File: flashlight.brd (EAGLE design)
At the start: 33 x 33 mm, 2 parts

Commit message: version 2 of the top board
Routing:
- net N$5: track 0.00 -> 106.7 mm, vias 1 -> 0
- net N$14: track 0.00 -> 13.2 mm, vias 1 -> 2
- net N$2: track 8.13 -> 0.00 mm
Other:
- board size 33 x 33 mm -> 33.2 x 17.8 mm
- board text added: "Top Board Rev. 2.0"
- board text removed: "Rev. 1.1"
- board text removed: "Top Board Rev. 1.1"
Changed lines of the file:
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@@
 <board>
 <plain>
-<circle x="16.51" y="16.51" radius="16.51" width="0.040640625" layer="20"/>
-<circle x="16.51" y="16.51" radius="14.5542" width="3.937" layer="16"/>
-<circle x="16.51" y="16.51" radius="5.08" width="11.43" layer="30"/>
+<circle x="16.51" y="16.51" radius="1.27" width="11.43" layer="30"/>
 <text x="16.51" y="20.32" size="1.778" layer="25" align="bottom-center">Stockton
 Flashlight</text>
-<circle x="16.51" y="16.51" radius="14.7574" width="3.556" layer="30"/>
-<circle x="16.51" y="16.51" radius="5.08" width="12.7" layer="16"/>
-<rectangle x1="6.35" y1="19.685" x2="26.67" y2="25.4" layer="1"/>
-<rectangle x1="6.35" y1="7.62" x2="26.67" y2="13.335" layer="1"/>
-<text x="16.51" y="3.81" size="1.778" layer="1" align="bottom-center">Rev. 1.1</text>
-<text x="16.51" y="3.81" size="1.778" layer="25" align="bottom-center">Top Board
-Rev. 1.1</text>
+<circle x="16.51" y="16.51" radius="0.762" width="12.7" layer="16"/>
+<rectangle x1="6.35" y1="19.685" x2="26.67" y2="22.86" layer="1"/>
+<rectangle x1="6.35" y1="10.16" x2="26.67" y2="13.335" layer="1"/>
+<text x="16.51" y="9.398" size="1.778" layer="25" align="bottom-center">Top Board
+Rev. 2.0</text>
 <rectangle x1="16" y1="13.2" x2="17" y2="19.7" layer="1"/>
 <text x="19.2" y="14.6" size="1.778" layer="25">+</text>
@@
 <rectangle x1="31.242" y1="15.24" x2="33.02" y2="17.78" layer="1"/>
 <rectangle x1="31.75" y1="15.24" x2="33.02" y2="17.78" layer="29"/>
-<circle x="16.51" y="16.51" radius="14.810615625" width="1.6256" layer="1"/>
+<wire x1="2.54" y1="25.4" x2="2.54" y2="7.62" width="0.0508" layer="20" curve="64.94"/>
+<wire x1="30.48" y1="25.4" x2="30.48" y2="7.62" width="0.0508" layer="20" curve="-65.94"/>
+<wire x1="2.54" y1="25.4" x2="30.48" y2="25.4" width="0.0508" layer="20"/>
+<wire x1="2.54" y1="7.62" x2="30.48" y2="7.62" width="0.0508" layer="20"/>
+<rectangle x1="4.064" y1="7.62" x2="29.21" y2="8.89" layer="1"/>
+<rectangle x1="4.318" y1="24.13" x2="28.702" y2="25.4" layer="1"/>
+<rectangle x1="4.318" y1="24.13" x2="28.702" y2="25.654" layer="16"/>
+<rectangle x1="4.318" y1="7.366" x2="28.702" y2="8.89" layer="16"/>
+<wire x1="4.572" y1="25.4" x2="4.572" y2="7.62" width="3.556" layer="30" curve="73.34"/>
+<wire x1="28.448" y1="25.4" x2="28.448" y2="7.62" width="3.556" layer="30" curve="-73.34"/>
+<rectangle x1="4.318" y1="7.366" x2="28.956" y2="8.89" layer="30"/>
+<rectangle x1="4.318" y1="24.13" x2="28.448" y2="25.654" layer="30"/>
 </plain>
 <attributes>
@@
 </autorouter>
 <elements>
-<element name="R1" library="resistor" package="R2010" value="" x="8.89" y="16.51" rot="R180"/>
+<element name="R1" library="resistor" package="R2010" value="" x="8.89" y="16.51" smashed="yes" rot="R180">
+<attribute name="NAME" x="10.541" y="19.685" size="1.27" layer="25" rot="R180"/>
+<attribute name="VALUE" x="11.049" y="19.431" size="1.27" layer="27" rot="R180"/>
+</element>
 <element name="LED1" library="led" package="ML-E" value="ML-E" x="16.5" y="16.5"/>
 </elements>
@@
 <via x="3.302" y="16.51" extent="1-16" drill="0.6"/>
 </signal>
-<signal name="N$2">
-<via x="26.67" y="16.51" extent="1-16" drill="0.6"/>
-<wire x1="26.67" y1="16.51" x2="18.542" y2="16.51" width="1.6256" layer="1"/>
-</signal>
 <signal name="N$3">
 <contactref element="R1" pad="1"/>
@@
 <via x="31.115" y="16.51" extent="1-16" drill="0.6"/>
 </signal>
-<signal name="N$5">
-<via x="16.51" y="31.75" extent="1-16" drill="0.6"/>
-</signal>
-<signal name="N$6">
-<via x="16.51" y="1.27" extent="1-16" drill="0.6"/>
-</signal>
-<signal name="N$7">
-<via x="5.08" y="26.67" extent="1-16" drill="0.6"/>
-</signal>
-<signal name="N$8">
-<via x="27.94" y="26.67" extent="1-16" drill="0.6"/>
-</signal>
-<signal name="N$9">
-<via x="27.94" y="6.35" extent="1-16" drill="0.6"/>
-</signal>
-<signal name="N$10">
-<via x="5.08" y="6.35" extent="1-16" drill="0.6"/>
-</signal>
 <signal name="N$11">
 <wire x1="15.24" y1="20.32" x2="16.51" y2="19.05" width="0.4064" layer="1"/>
@@
 <signal name="N$14">
 <via x="21.59" y="16.51" extent="1-16" drill="0.6"/>
+<via x="26.67" y="16.51" extent="1-16" drill="0.6"/>
+<wire x1="26.67" y1="16.51" x2="18.542" y2="16.51" width="1.6256" layer="1"/>
+<wire x1="26.67" y1="16.51" x2="21.59" y2="16.51" width="2.54" layer="16"/>
 </signal>
 <signal name="N$15">
@@
 <wire x1="32.512" y1="15.494" x2="31.75" y2="14.732" width="0.4064" layer="1"/>
 </signal>
+<signal name="N$5">
+<wire x1="4.572" y1="25.4" x2="4.572" y2="7.62" width="1.524" layer="1" curve="73.34"/>
+<wire x1="28.448" y1="25.4" x2="28.448" y2="7.62" width="1.524" layer="1" curve="-73.34"/>
+<wire x1="4.572" y1="25.4" x2="4.572" y2="7.62" width="1.524" layer="1" curve="73.34"/>
+<wire x1="4.572" y1="25.4" x2="4.572" y2="7.62" width="1.524" layer="1" curve="73.34"/>
+<wire x1="28.448" y1="7.62" x2="28.448" y2="25.4" width="3.556" layer="16" curve="73.34"/>
+<wire x1="4.572" y1="25.4" x2="4.572" y2="7.62" width="3.556" layer="16" curve="73.34"/>
+<wire x1="28.448" y1="7.62" x2="28.448" y2="7.62" width="0" layer="19" extent="1-16"/>
+<wire x1="4.572" y1="25.4" x2="28.448" y2="25.4" width="0" layer="19" extent="1-1"/>
+<wire x1="-0.508" y1="25.4" x2="4.572" y2="25.4" width="0" layer="19" extent="1-16"/>
+<wire x1="4.572" y1="25.4" x2="-0.508" y2="25.4" width="0" layer="19" extent="16-16"/>
+<wire x1="-10.668" y1="25.4" x2="4.572" y2="25.4" width="0" layer="19" extent="16-16"/>
+</signal>
+<signal name="N$2">
+<via x="2.54" y="20.32" extent="1-16" drill="0.6"/>
+</signal>
+<signal name="N$6">
+<via x="4.318" y="24.13" extent="1-16" drill="0.6"/>
+</signal>
+<signal name="N$7">
+<via x="2.54" y="12.7" extent="1-16" drill="0.6"/>
+</signal>
+<signal name="N$8">
+<via x="4.318" y="8.89" extent="1-16" drill="0.6"/>
+</signal>
+<signal name="N$9">
+<via x="30.48" y="12.7" extent="1-16" drill="0.6"/>
+</signal>
+<signal name="N$10">
+<via x="30.48" y="20.32" extent="1-16" drill="0.6"/>
+</signal>
+<signal name="N$20">
+<via x="28.702" y="24.13" extent="1-16" drill="0.6"/>
+</signal>
+<signal name="N$21">
+<via x="28.702" y="8.89" extent="1-16" drill="0.6"/>
+</signal>
+<signal name="N$22">
+<via x="16.51" y="25.4" extent="1-16" drill="0.6"/>
+</signal>
+<signal name="N$23">
+<via x="16.51" y="7.62" extent="1-16" drill="0.6"/>
+</signal>
+<signal name="N$24">
+<via x="10.16" y="7.62" extent="1-16" drill="0.6"/>
+</signal>
+<signal name="N$25">
+<via x="22.86" y="7.62" extent="1-16" drill="0.6"/>
+</signal>
+<signal name="N$26">
+<via x="10.16" y="25.4" extent="1-16" drill="0.6"/>
+</signal>
+<signal name="N$27">
+<via x="22.86" y="25.4" extent="1-16" drill="0.6"/>
+</signal>
 </signals>

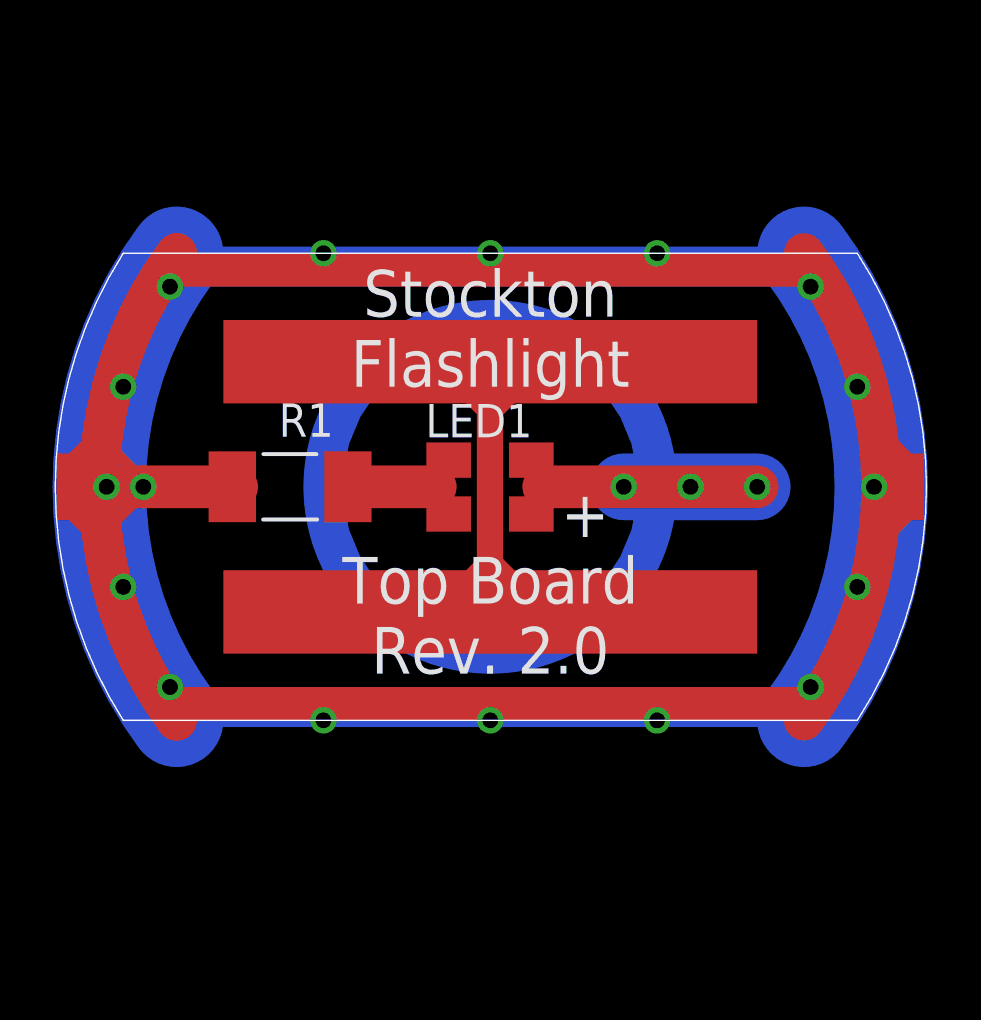
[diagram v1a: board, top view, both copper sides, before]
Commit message: rev 2.0 of the bottom board, plus minor tweaks to the top board
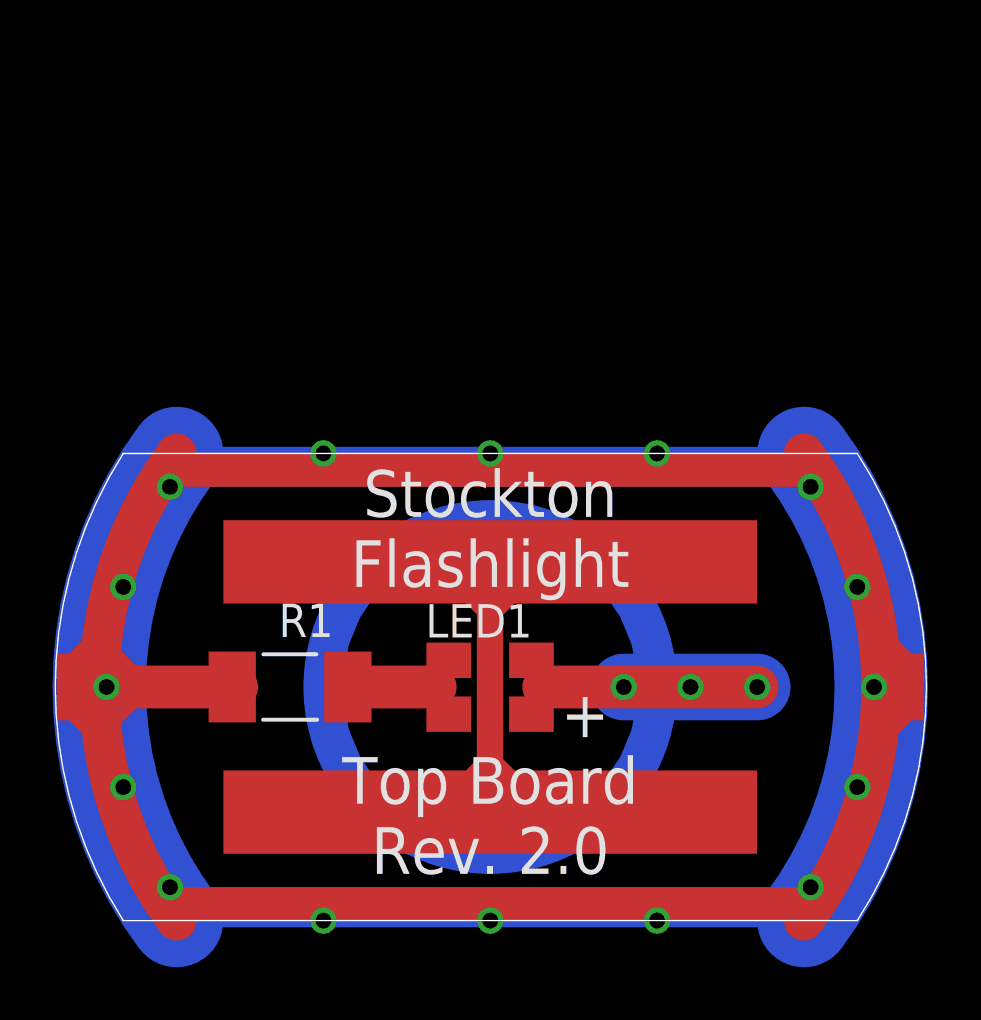
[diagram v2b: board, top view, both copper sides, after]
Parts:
- moved R1 7.62 mm to (8.89, 8.89)
- moved LED1 7.62 mm to (16.5, 8.88)
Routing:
- net N$5: track 106.7 -> 71.1 mm
- net N$1: vias 2 -> 1

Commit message: top board rev 3 (with the 350ma reg)
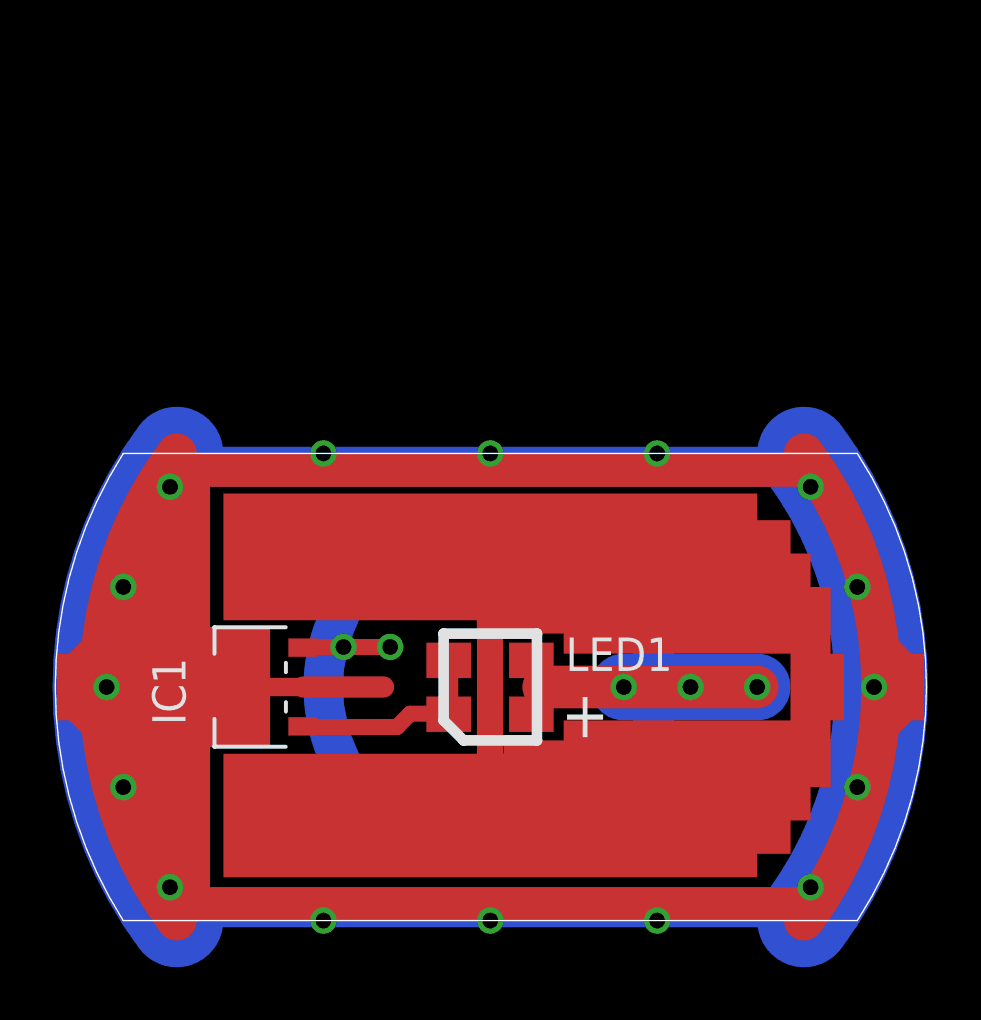
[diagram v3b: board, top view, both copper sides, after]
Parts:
- removed R1: (no value), resistor:R2010
- added IC1: AMC7135SOT-89, esoteric-regulators:SOT89-R
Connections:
- new net GND: IC1.3
- new net N$28: IC1.2, LED1.A@1
- net N$3: now also IC1.1; no longer R1.1
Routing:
- net N$3: track 4.48 -> 0.00 mm
- net N$12: track 3.59 -> 7.83 mm
- net N$29: track 0.00 -> 3.30 mm, vias 0 -> 2
- net N$30: track 0.00 -> 3.05 mm
- net N$1: track 4.95 -> 3.17 mm
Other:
- board text added: "Top Board Rev. 3.0"
- board text removed: "Top Board Rev. 2.0"
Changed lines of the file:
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@@
 <plain>
 <circle x="16.51" y="8.89" radius="1.27" width="11.43" layer="30"/>
-<text x="16.51" y="12.7" size="1.778" layer="25" align="bottom-center">Stockton
+<text x="16.51" y="11.684" size="1.778" layer="29" align="bottom-center">Stockton
 Flashlight</text>
 <circle x="16.51" y="8.89" radius="0.762" width="12.7" layer="16"/>
-<rectangle x1="6.35" y1="12.065" x2="26.67" y2="15.24" layer="1"/>
-<rectangle x1="6.35" y1="2.54" x2="26.67" y2="5.715" layer="1"/>
-<text x="16.51" y="1.778" size="1.778" layer="25" align="bottom-center">Top Board
-Rev. 2.0</text>
+<rectangle x1="6.35" y1="11.43" x2="26.67" y2="16.256" layer="1"/>
+<rectangle x1="6.35" y1="1.651" x2="26.67" y2="6.35" layer="1"/>
+<text x="16.51" y="1.778" size="1.778" layer="29" align="bottom-center">Top Board
+Rev. 3.0</text>
 <rectangle x1="16" y1="5.58" x2="17" y2="12.08" layer="1"/>
 <text x="19.2" y="6.98" size="1.778" layer="25">+</text>
@@
 <wire x1="4.572" y1="17.78" x2="4.572" y2="0" width="3.556" layer="30" curve="73.34" cap="flat"/>
 <wire x1="28.448" y1="17.78" x2="28.448" y2="0" width="3.556" layer="30" curve="-73.34" cap="flat"/>
-<rectangle x1="4.318" y1="-0.254" x2="28.956" y2="1.27" layer="30"/>
-<rectangle x1="4.318" y1="16.51" x2="28.448" y2="18.034" layer="30"/>
+<rectangle x1="3.302" y1="0.762" x2="5.842" y2="16.51" layer="1"/>
+<rectangle x1="2.032" y1="3.81" x2="3.81" y2="13.97" layer="1"/>
+<rectangle x1="5.842" y1="6.604" x2="8.128" y2="11.176" layer="1"/>
+<rectangle x1="16.002" y1="10.922" x2="26.67" y2="11.43" layer="1"/>
+<rectangle x1="17.018" y1="6.35" x2="26.67" y2="6.858" layer="1"/>
+<rectangle x1="19.304" y1="10.16" x2="26.67" y2="10.922" layer="1"/>
+<rectangle x1="19.304" y1="6.858" x2="26.67" y2="7.62" layer="1"/>
+<rectangle x1="26.67" y1="2.54" x2="27.94" y2="7.62" layer="1"/>
+<rectangle x1="26.67" y1="10.16" x2="27.94" y2="15.24" layer="1"/>
+<rectangle x1="27.94" y1="5.08" x2="29.464" y2="12.7" layer="1"/>
+<rectangle x1="27.94" y1="3.81" x2="28.702" y2="5.08" layer="1"/>
+<rectangle x1="27.94" y1="12.7" x2="28.702" y2="13.97" layer="1"/>
+<rectangle x1="29.464" y1="7.62" x2="29.972" y2="10.16" layer="1"/>
+<wire x1="14.732" y1="10.922" x2="18.288" y2="10.922" width="0.4064" layer="25"/>
+<wire x1="18.288" y1="10.922" x2="18.288" y2="6.858" width="0.4064" layer="25"/>
+<wire x1="18.288" y1="6.858" x2="15.494" y2="6.858" width="0.4064" layer="25"/>
+<wire x1="15.494" y1="6.858" x2="14.732" y2="7.62" width="0.4064" layer="25"/>
+<wire x1="14.732" y1="7.62" x2="14.732" y2="10.922" width="0.4064" layer="25"/>
 </plain>
 <attributes>
@@
 </autorouter>
 <elements>
-<element name="R1" library="resistor" package="R2010" value="" x="8.89" y="8.89" smashed="yes" rot="R180">
-<attribute name="NAME" x="10.541" y="12.065" size="1.27" layer="25" rot="R180"/>
-<attribute name="VALUE" x="11.049" y="11.811" size="1.27" layer="27" rot="R180"/>
+<element name="LED1" library="led" package="ML-E" value="ML-E" x="16.5" y="8.88" smashed="yes">
+<attribute name="NAME" x="19.3764" y="9.5034" size="1.27" layer="25"/>
+<attribute name="VALUE" x="-5.2086" y="2.6124" size="1.27" layer="27" rot="R90"/>
 </element>
-<element name="LED1" library="led" package="ML-E" value="ML-E" x="16.5" y="8.88"/>
+<element name="IC1" library="esoteric-regulators" package="SOT89-R" value="AMC7135SOT-89" x="7.62" y="8.89" smashed="yes" rot="R90">
+<attribute name="NAME" x="4.911" y="7.447" size="1.27" layer="25" rot="R90"/>
+<attribute name="VALUE" x="-7.605" y="2.875" size="1.27" layer="27" rot="R90"/>
+</element>
 </elements>
 <signals>
 <signal name="N$1">
 <via x="1.905" y="8.89" extent="1-16" drill="0.6"/>
-<wire x1="6.858" y1="8.89" x2="1.905" y2="8.89" width="1.6256" layer="1"/>
-</signal>
-<signal name="N$3">
-<contactref element="R1" pad="1"/>
-<contactref element="LED1" pad="C@1"/>
-<wire x1="11.09" y1="8.89" x2="14.417" y2="8.89" width="1.6256" layer="1"/>
-<wire x1="14.417" y1="8.89" x2="14.925" y2="7.855" width="0.4064" layer="1"/>
+<wire x1="5.08" y1="8.89" x2="1.905" y2="8.89" width="1.6256" layer="1"/>
 </signal>
 <signal name="N$4">
@@
 <wire x1="15.24" y1="12.7" x2="16.51" y2="11.43" width="0.4064" layer="1"/>
 <wire x1="16.51" y1="11.43" x2="17.78" y2="12.7" width="0.4064" layer="1"/>
-</signal>
-<signal name="N$12">
-<wire x1="15.24" y1="5.08" x2="16.51" y2="6.35" width="0.4064" layer="1"/>
-<wire x1="16.51" y1="6.35" x2="17.78" y2="5.08" width="0.4064" layer="1"/>
 </signal>
 <signal name="N$13">
@@
 <via x="22.86" y="17.78" extent="1-16" drill="0.6"/>
 </signal>
+<signal name="GND">
+<contactref element="IC1" pad="3"/>
+</signal>
+<signal name="N$3">
+<contactref element="LED1" pad="C@1"/>
+<contactref element="IC1" pad="1"/>
+<wire x1="9.37" y1="10.39" x2="14.925" y2="7.855" width="0" layer="19" extent="1-1"/>
+</signal>
+<signal name="N$28">
+<contactref element="LED1" pad="A@1"/>
+<contactref element="IC1" pad="2"/>
+<wire x1="9.37" y1="7.39" x2="18.075" y2="7.855" width="0" layer="19" extent="1-1"/>
+</signal>
+<signal name="N$12">
+<wire x1="9.398" y1="7.366" x2="12.954" y2="7.366" width="0.6096" layer="1"/>
+<wire x1="12.954" y1="7.366" x2="13.462" y2="7.874" width="0.6096" layer="1"/>
+<wire x1="13.462" y1="7.874" x2="14.986" y2="7.874" width="0.6096" layer="1"/>
+<wire x1="14.986" y1="7.874" x2="14.986" y2="9.906" width="0.6096" layer="1"/>
+</signal>
+<signal name="N$29">
+<wire x1="9.398" y1="10.414" x2="10.922" y2="10.414" width="0.6096" layer="1"/>
+<wire x1="10.922" y1="10.414" x2="12.7" y2="10.414" width="0.6096" layer="1"/>
+<via x="10.922" y="10.414" extent="1-16" drill="0.6"/>
+<via x="12.7" y="10.414" extent="1-16" drill="0.6"/>
+</signal>
+<signal name="N$30">
+<wire x1="9.398" y1="8.89" x2="12.446" y2="8.89" width="0.8128" layer="1"/>
+</signal>
 </signals>
